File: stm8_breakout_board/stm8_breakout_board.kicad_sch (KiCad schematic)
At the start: 23 parts, among them J1 STLinkV2 Connector, J2 Conn_01x10_Male, J3 Power Connector, J4 Conn_01x10_Male, SW1 Reset, U1 STM8S003F3P, U2 XC6206, U3 AMS1117-3.3

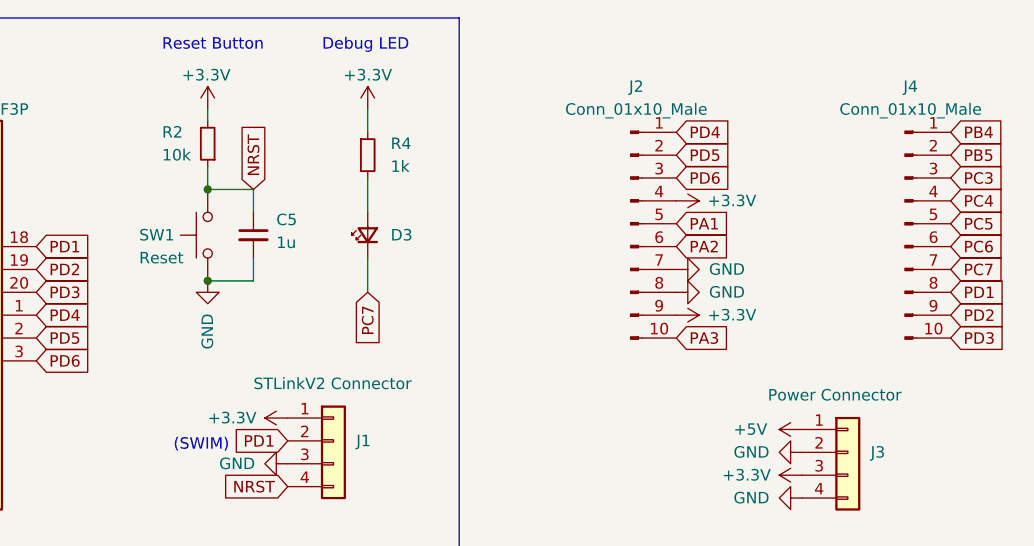
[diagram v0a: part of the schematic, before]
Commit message: as-ordered boards
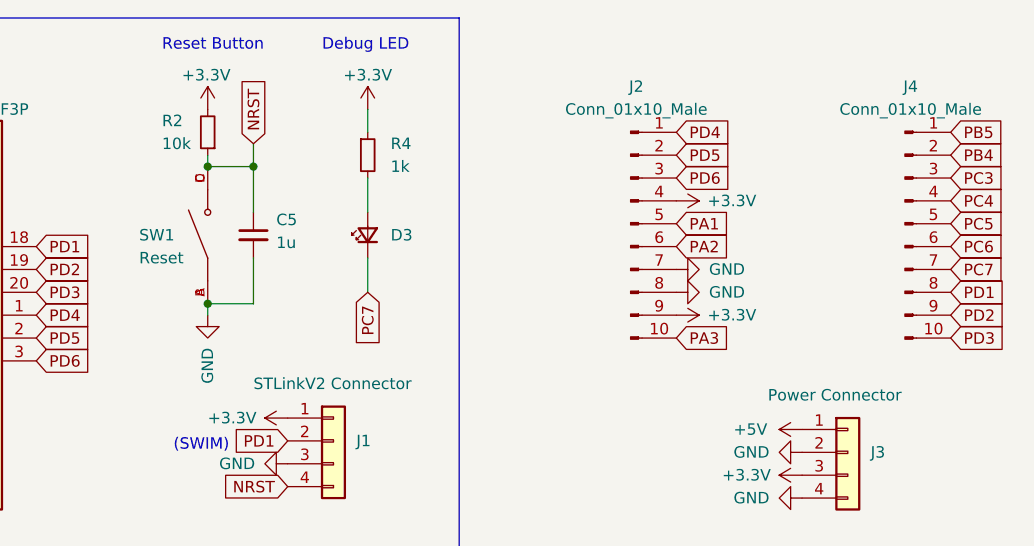
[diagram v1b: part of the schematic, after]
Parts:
- SW1: footprint Button_Switch_THT:SW_PUSH_6mm_H4.3mm -> SW_TS-1187A-B-A-B; symbol Switch:SW_Push -> TS-1187A-B-A-B:TS-1187A-B-A-B; LCSC DNP -> C318884; MANUFACTURER (none) -> XKB Industrial Precision; MAXIMUM_PACKAGE_HEIGHT (none) -> 1.5mm; PARTREV (none) -> A0; STANDARD (none) -> Manufacturer Recommendations
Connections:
- net GND: now also SW1.A, SW1.B; no longer SW1.1
- net NRST: now also SW1.C, SW1.D; no longer SW1.2
- net PB4: now also J4.2 (Pin_2); no longer J4.1 (Pin_1)
- net PB5: now also J4.1 (Pin_1); no longer J4.2 (Pin_2)
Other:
- moved on the sheet: R2
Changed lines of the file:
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@@
   (junction (at 43.18 90.17) (diameter 0) (color 0 0 0 0)
   )
+  (junction (at 87.63 33.02) (diameter 0) (color 0 0 0 0)
+  )
   (junction (at 87.63 90.17) (diameter 0) (color 0 0 0 0)
   )
+  (junction (at 82.55 48.26) (diameter 0) (color 0 0 0 0)
+  )
+  (junction (at 82.55 33.02) (diameter 0) (color 0 0 0 0)
+  )
   (junction (at 97.79 90.17) (diameter 0) (color 0 0 0 0)
   )
@@
   (junction (at 54.61 99.06) (diameter 0) (color 0 0 0 0)
   )
-  (junction (at 82.55 35.56) (diameter 0) (color 0 0 0 0)
-  )
-  (junction (at 82.55 45.72) (diameter 0) (color 0 0 0 0)
-  )
-  (wire (pts (xy 82.55 45.72) (xy 87.63 45.72))
+  (wire (pts (xy 87.63 33.02) (xy 87.63 38.1))
+    (stroke (width 0) (type default) (color 0 0 0 0))
+  )
+  (wire (pts (xy 82.55 48.26) (xy 87.63 48.26))
     (stroke (width 0) (type default) (color 0 0 0 0))
   )
@@
     (stroke (width 0) (type default) (color 0 0 0 0))
   )
-  (wire (pts (xy 87.63 35.56) (xy 87.63 38.1))
-    (stroke (width 0) (type default) (color 0 0 0 0))
-  )
   (wire (pts (xy 39.37 149.86) (xy 44.45 149.86))
     (stroke (width 0) (type default) (color 0 0 0 0))
@@
     (stroke (width 0) (type default) (color 0 0 0 0))
   )
-  (wire (pts (xy 82.55 33.02) (xy 82.55 35.56))
-    (stroke (width 0) (type default) (color 0 0 0 0))
-  )
   (wire (pts (xy 45.72 22.86) (xy 48.26 22.86))
     (stroke (width 0) (type default) (color 0 0 0 0))
@@
     (stroke (width 0) (type default) (color 0 0 0 0))
   )
-  (wire (pts (xy 87.63 43.18) (xy 87.63 45.72))
+  (wire (pts (xy 87.63 43.18) (xy 87.63 48.26))
     (stroke (width 0) (type default) (color 0 0 0 0))
   )
@@
     (stroke (width 0) (type default) (color 0 0 0 0))
   )
-  (wire (pts (xy 82.55 26.67) (xy 82.55 27.94))
-    (stroke (width 0) (type default) (color 0 0 0 0))
-  )
   (wire (pts (xy 45.72 74.93) (xy 48.26 74.93))
     (stroke (width 0) (type default) (color 0 0 0 0))
   )
+  (wire (pts (xy 82.55 33.02) (xy 87.63 33.02))
+    (stroke (width 0) (type default) (color 0 0 0 0))
+  )
   (polyline (pts (xy 110.49 77.47) (xy 110.49 16.51))
     (stroke (width 0) (type default) (color 0 0 0 0))
@@
     (stroke (width 0) (type default) (color 0 0 0 0))
   )
+  (wire (pts (xy 82.55 31.75) (xy 82.55 33.02))
+    (stroke (width 0) (type default) (color 0 0 0 0))
+  )
   (wire (pts (xy 87.63 99.06) (xy 78.74 99.06))
     (stroke (width 0) (type default) (color 0 0 0 0))
@@
     (stroke (width 0) (type default) (color 0 0 0 0))
   )
-  (wire (pts (xy 82.55 35.56) (xy 87.63 35.56))
+  (wire (pts (xy 82.55 48.26) (xy 82.55 49.53))
     (stroke (width 0) (type default) (color 0 0 0 0))
   )
   (wire (pts (xy 54.61 97.79) (xy 54.61 99.06))
+    (stroke (width 0) (type default) (color 0 0 0 0))
+  )
+  (wire (pts (xy 87.63 30.48) (xy 87.63 33.02))
     (stroke (width 0) (type default) (color 0 0 0 0))
   )
@@
     )
   )
-  (global_label "PB5" (shape input) (at 165.1 31.75 0) (fields_autoplaced)
-    (effects (font (size 1.27 1.27)) (justify left))
-    (property "Intersheet References" "${INTERSHEET_REFS}" (id 0) (at 171.2626 31.6706 0)
+  (global_label "PB5" (shape input) (at 165.1 29.21 0) (fields_autoplaced)
+    (effects (font (size 1.27 1.27)) (justify left))
+    (property "Intersheet References" "${INTERSHEET_REFS}" (id 0) (at 171.2626 29.1306 0)
       (effects (font (size 1.27 1.27)) (justify left) hide)
     )
@@
     )
   )
-  (global_label "PB4" (shape input) (at 165.1 29.21 0) (fields_autoplaced)
-    (effects (font (size 1.27 1.27)) (justify left))
-    (property "Intersheet References" "${INTERSHEET_REFS}" (id 0) (at 171.2626 29.1306 0)
+  (global_label "PB4" (shape input) (at 165.1 31.75 0) (fields_autoplaced)
+    (effects (font (size 1.27 1.27)) (justify left))
+    (property "Intersheet References" "${INTERSHEET_REFS}" (id 0) (at 171.2626 31.6706 0)
       (effects (font (size 1.27 1.27)) (justify left) hide)
     )
@@
     )
   )
-  (global_label "NRST" (shape input) (at 87.63 35.56 90) (fields_autoplaced)
-    (effects (font (size 1.27 1.27)) (justify left))
-    (property "Intersheet References" "${INTERSHEET_REFS}" (id 0) (at 87.7094 28.3693 90)
+  (global_label "NRST" (shape input) (at 87.63 30.48 90) (fields_autoplaced)
+    (effects (font (size 1.27 1.27)) (justify left))
+    (property "Intersheet References" "${INTERSHEET_REFS}" (id 0) (at 87.7094 23.2893 90)
       (effects (font (size 1.27 1.27)) (justify left) hide)
     )
@@
     (pin "1")
   )
-  (symbol (lib_id "power:GND") (at 82.55 45.72 0) (unit 1)
-    (in_bom yes) (on_board yes)
-    (property "Reference" "#PWR015" (id 0) (at 82.55 52.07 0)
-      (effects (font (size 1.27 1.27)) hide)
-    )
-    (property "Value" "GND" (id 1) (at 82.55 53.34 90)
-      (effects (font (size 1.27 1.27)) (justify left))
-    )
-    (property "Footprint" "" (id 2) (at 82.55 45.72 0)
-      (effects (font (size 1.27 1.27)) hide)
-    )
-    (property "Datasheet" "" (id 3) (at 82.55 45.72 0)
+  (symbol (lib_id "power:GND") (at 82.55 49.53 0) (unit 1)
+    (in_bom yes) (on_board yes)
+    (property "Reference" "#PWR015" (id 0) (at 82.55 55.88 0)
+      (effects (font (size 1.27 1.27)) hide)
+    )
+    (property "Value" "GND" (id 1) (at 82.55 57.15 90)
+      (effects (font (size 1.27 1.27)) (justify left))
+    )
+    (property "Footprint" "" (id 2) (at 82.55 49.53 0)
+      (effects (font (size 1.27 1.27)) hide)
+    )
+    (property "Datasheet" "" (id 3) (at 82.55 49.53 0)
       (effects (font (size 1.27 1.27)) hide)
     )
@@
     (pin "1")
   )
-  (symbol (lib_id "Switch:SW_Push") (at 82.55 40.64 90) (unit 1)
+  (symbol (lib_id "TS-1187A-B-A-B:TS-1187A-B-A-B") (at 82.55 40.64 90) (unit 1)
     (in_bom yes) (on_board yes)
     (property "Reference" "SW1" (id 0) (at 74.93 40.64 90)
@@
       (effects (font (size 1.27 1.27)) (justify right))
     )
-    (property "Footprint" "Button_Switch_THT:SW_PUSH_6mm_H4.3mm" (id 2) (at 77.47 40.64 0)
-      (effects (font (size 1.27 1.27)) hide)
-    )
-    (property "Datasheet" "~" (id 3) (at 77.47 40.64 0)
-      (effects (font (size 1.27 1.27)) hide)
-    )
-    (property "LCSC" "DNP" (id 4) (at 82.55 40.64 0)
-      (effects (font (size 1.27 1.27)) hide)
-    )
-    (pin "1")
-    (pin "2")
+    (property "Footprint" "SW_TS-1187A-B-A-B" (id 2) (at 82.55 40.64 0)
+      (effects (font (size 1.27 1.27)) (justify left bottom) hide)
+    )
+    (property "Datasheet" "~" (id 3) (at 82.55 40.64 0)
+      (effects (font (size 1.27 1.27)) (justify left bottom) hide)
+    )
+    (property "LCSC" "C318884" (id 4) (at 82.55 40.64 0)
+      (effects (font (size 1.27 1.27)) hide)
+    )
+    (property "STANDARD" "Manufacturer Recommendations" (id 5) (at 82.55 40.64 0)
+      (effects (font (size 1.27 1.27)) (justify left bottom) hide)
+    )
+    (property "MANUFACTURER" "XKB Industrial Precision" (id 6) (at 82.55 40.64 0)
+      (effects (font (size 1.27 1.27)) (justify left bottom) hide)
+    )
+    (property "PARTREV" "A0" (id 7) (at 82.55 40.64 0)
+      (effects (font (size 1.27 1.27)) (justify left bottom) hide)
+    )
+    (property "MAXIMUM_PACKAGE_HEIGHT" "1.5mm" (id 8) (at 82.55 40.64 0)
+      (effects (font (size 1.27 1.27)) (justify left bottom) hide)
+    )
+    (pin "A")
+    (pin "B")
+    (pin "C")
+    (pin "D")
   )
   (symbol (lib_id "Connector:Conn_01x10_Male") (at 129.54 39.37 0) (unit 1)
@@
     (pin "9")
   )
-  (symbol (lib_id "Device:R_Small") (at 82.55 30.48 180) (unit 1)
-    (in_bom yes) (on_board yes)
-    (property "Reference" "R2" (id 0) (at 77.47 29.21 0)
-      (effects (font (size 1.27 1.27)) (justify right))
-    )
-    (property "Value" "10k" (id 1) (at 77.47 31.75 0)
-      (effects (font (size 1.27 1.27)) (justify right))
-    )
-    (property "Footprint" "Resistor_SMD:R_0603_1608Metric" (id 2) (at 82.55 30.48 0)
-      (effects (font (size 1.27 1.27)) hide)
-    )
-    (property "Datasheet" "~" (id 3) (at 82.55 30.48 0)
-      (effects (font (size 1.27 1.27)) hide)
-    )
-    (property "DigikeyPN" "" (id 4) (at 82.55 30.48 0)
-      (effects (font (size 1.27 1.27)) hide)
-    )
-    (property "LCSC" "C25804" (id 5) (at 82.55 30.48 0)
+  (symbol (lib_id "Device:R_Small") (at 82.55 29.21 180) (unit 1)
+    (in_bom yes) (on_board yes)
+    (property "Reference" "R2" (id 0) (at 77.47 27.94 0)
+      (effects (font (size 1.27 1.27)) (justify right))
+    )
+    (property "Value" "10k" (id 1) (at 77.47 30.48 0)
+      (effects (font (size 1.27 1.27)) (justify right))
+    )
+    (property "Footprint" "Resistor_SMD:R_0603_1608Metric" (id 2) (at 82.55 29.21 0)
+      (effects (font (size 1.27 1.27)) hide)
+    )
+    (property "Datasheet" "~" (id 3) (at 82.55 29.21 0)
+      (effects (font (size 1.27 1.27)) hide)
+    )
+    (property "DigikeyPN" "" (id 4) (at 82.55 29.21 0)
+      (effects (font (size 1.27 1.27)) hide)
+    )
+    (property "LCSC" "C25804" (id 5) (at 82.55 29.21 0)
       (effects (font (size 1.27 1.27)) hide)
     )
@@
     )
     (path "/91c9d0a5-a998-4e04-a89a-86f0aa8dad26"
-      (reference "SW1") (unit 1) (value "Reset") (footprint "Button_Switch_THT:SW_PUSH_6mm_H4.3mm")
+      (reference "SW1") (unit 1) (value "Reset") (footprint "SW_TS-1187A-B-A-B")
     )
     (path "/6a329fcf-1e4c-49b6-860e-0b96de442f04"
